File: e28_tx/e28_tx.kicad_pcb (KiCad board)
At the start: 2 copper layers, 40.5 x 56 mm, 25 parts, among them J1 USB_B_Micro, J2 Conn_01x05, J3 Conn_01x04, J4 Conn_01x04, Q1 BC847BS, SW1 SW_Push, SW2 SW_Push, U1 CH340C, U2 me6211c33, U3 ESP32-WROOM-32D, U4 E28-2G4M27S

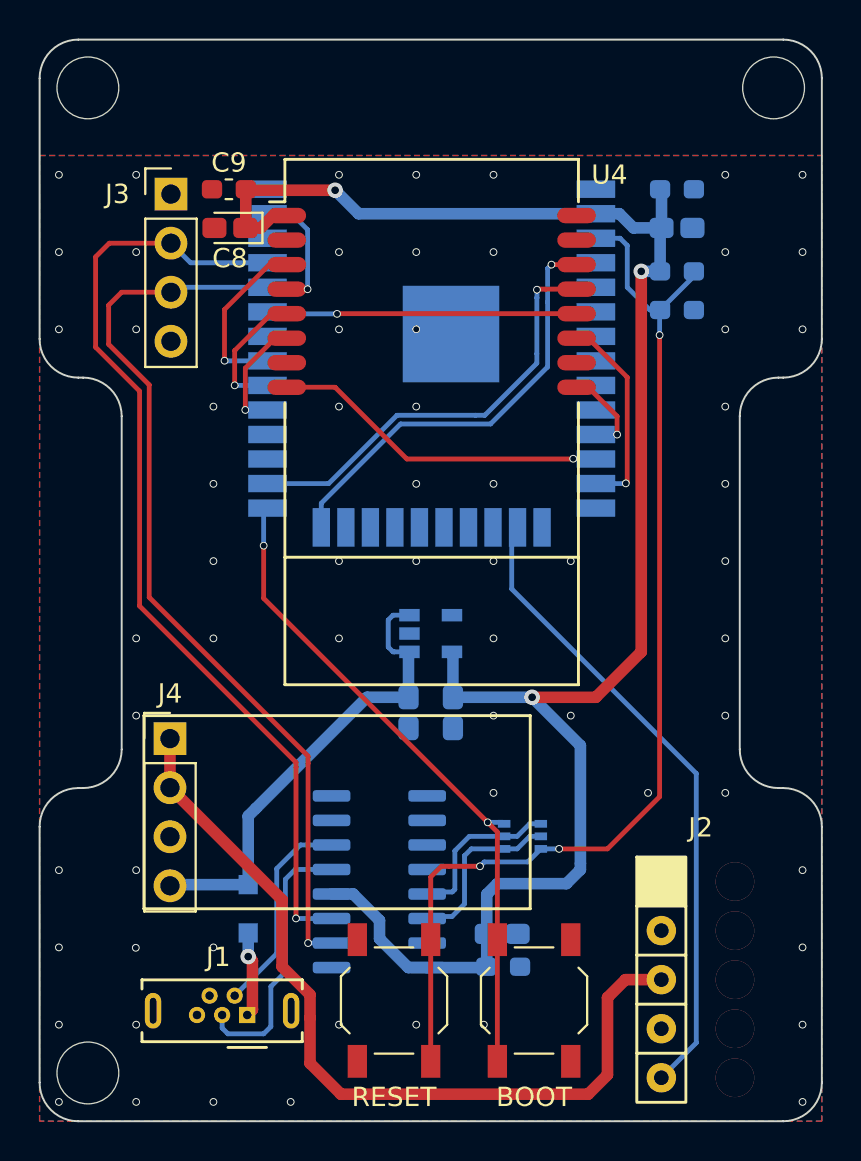
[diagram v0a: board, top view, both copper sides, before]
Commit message: Added minimal RX
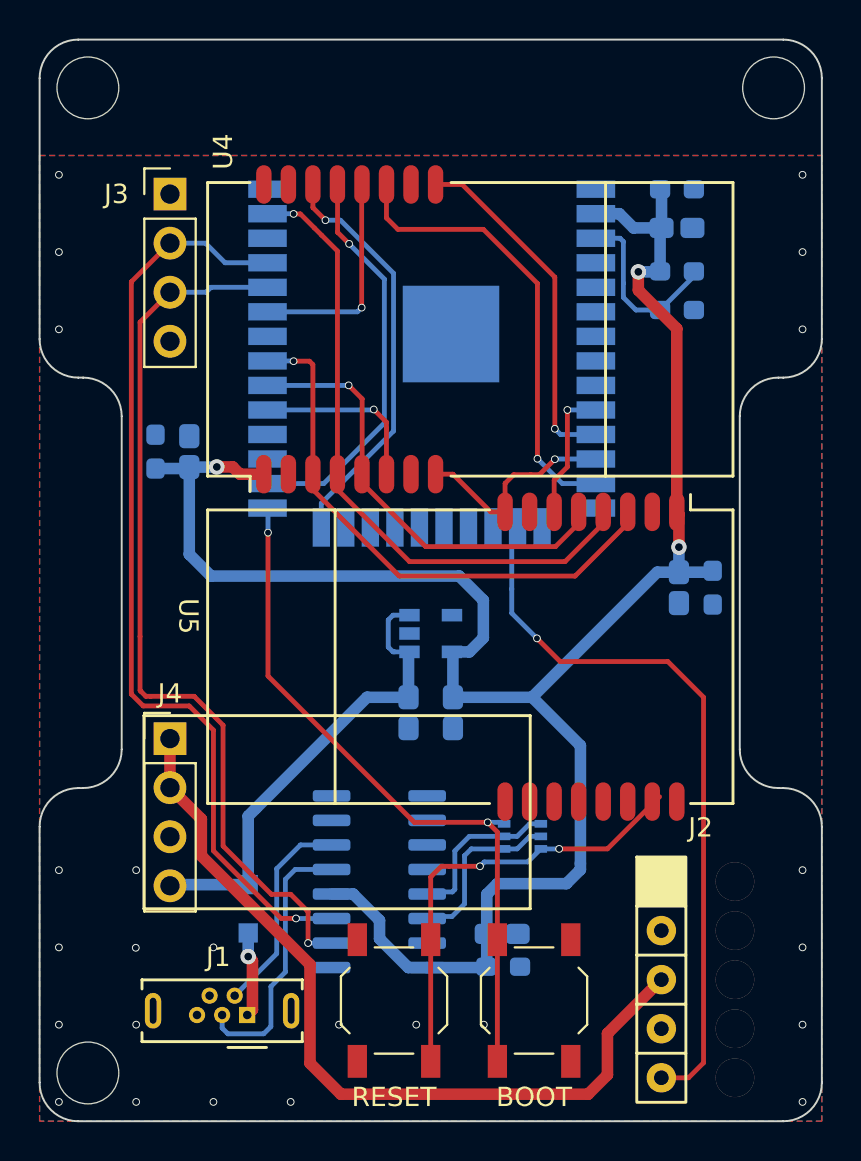
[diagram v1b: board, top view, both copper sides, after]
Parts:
- added C10: 10uF, Capacitor_Tantalum_SMD:CP_EIA-1608-08_AVX-J_Pad1.25x1.05mm_HandSolder, B.Cu at (133.1, 122.4)
- added C11: 100nF, Capacitor_SMD:C_0603_1608Metric_Pad1.05x0.95mm_HandSolder, B.Cu at (134.8, 122.4)
- added U5: E28-2G4M27S, ELRS_lib:E28-2G4M27S, F.Cu at (124.1, 126.0)
- C8, C9: moved to B.Cu
- moved C9 14.1 mm to (106.0, 115.3), turned to 90 degrees
- moved C8 11.8 mm to (107.8, 115.3), turned to 90 degrees
- moved U4 3.01 mm to (120.5, 109.0), turned to 90 degrees
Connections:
- net /DIO1 renamed /DIO11
- net /NSS renamed /NSS1
- J1 pad 4: Net-(J1-Pad4) -> (no net)
- J2 pad 1: Net-(J2-Pad1) -> (no net)
- J2 pad 2: Net-(J2-Pad2) -> (no net)
- J3 pad 1: Net-(J3-Pad1) -> (no net)
- U1 pad 10: Net-(U1-Pad10) -> (no net)
- U1 pad 11: Net-(U1-Pad11) -> (no net)
- U1 pad 12: Net-(U1-Pad12) -> (no net)
- U1 pad 15: Net-(U1-Pad15) -> (no net)
- U1 pad 7: Net-(U1-Pad7) -> (no net)
- U1 pad 8: Net-(U1-Pad8) -> (no net)
- U1 pad 9: Net-(U1-Pad9) -> (no net)
- U3 pad 10: Net-(U3-Pad10) -> /NSS2
- U3 pad 14: Net-(U3-Pad14) -> (no net)
- U3 pad 17: Net-(U3-Pad17) -> (no net)
- U3 pad 18: Net-(U3-Pad18) -> (no net)
- U3 pad 19: Net-(U3-Pad19) -> (no net)
- U3 pad 20: Net-(U3-Pad20) -> (no net)
- U3 pad 21: Net-(U3-Pad21) -> (no net)
- U3 pad 22: Net-(U3-Pad22) -> (no net)
- U3 pad 23: Net-(U3-Pad23) -> (no net)
- U3 pad 24: /DIO2 -> /DIO21
- U3 pad 27: Net-(U3-Pad27) -> /DIO21
- U3 pad 28: Net-(U3-Pad28) -> /DIO12
- U3 pad 32: Net-(U3-Pad32) -> (no net)
- U3 pad 36: Net-(U3-Pad36) -> (no net)
- U3 pad 4: Net-(U3-Pad4) -> (no net)
- U3 pad 5: Net-(U3-Pad5) -> (no net)
- U3 pad 6: Net-(U3-Pad6) -> (no net)
- U3 pad 7: Net-(U3-Pad7) -> (no net)
- U3 pad 8: Net-(U3-Pad8) -> (no net)
- U3 pad 9: Net-(U3-Pad9) -> (no net)
- U4 pad 14: /DIO2 -> /DIO21
- U4 pad 15: Net-(U4-Pad15) -> (no net)
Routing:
- net /MOSI: track 6.58 -> 33.5 mm
- net /RST: track 57.2 -> 32.4 mm, vias 3 -> 2
- net /DIO2: track 22.6 -> 0.00 mm, vias 1 -> 0
- net /DIO21: track 0.00 -> 21.5 mm, vias 0 -> 1
- net /MISO: track 9.07 -> 28.8 mm
- net /SCK: track 6.99 -> 23.2 mm
- net /TXEN: track 4.77 -> 18.3 mm
- net /RESET: track 10.5 -> 23.6 mm
- net +3V3: track 94.4 -> 104.1 mm
- net /NSS2: track 0.00 -> 7.03 mm, vias 0 -> 1
- net /RXEN: track 17.6 -> 11.1 mm
- net /BUSY: track 16.0 -> 11.3 mm
- net /SPORT: track 33.2 -> 37.6 mm, vias 0 -> 1
- net /NSS1: track 6.11 -> 9.13 mm
- net /BOOT: track 34.6 -> 36.7 mm
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
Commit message: Last tweaks and gerber files to min_sx1280 and e28_tx
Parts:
- removed C10: 10uF, Capacitor_Tantalum_SMD:CP_EIA-1608-08_AVX-J_Pad1.25x1.05mm_HandSolder
- removed C11: 100nF, Capacitor_SMD:C_0603_1608Metric_Pad1.05x0.95mm_HandSolder
- removed C3, C5: 2.2uF, Capacitor_Tantalum_SMD:CP_EIA-1608-08_AVX-J_Pad1.25x1.05mm_HandSolder
- removed U2: me6211c33, Package_TO_SOT_SMD:SOT-23-5
- removed U5: E28-2G4M27S, ELRS_lib:E28-2G4M27S
- C8, C9: moved to F.Cu
- H1, H2, H3: renamed from REF**; value MountingHole_3.2mm_M3 -> MountingHole
- moved C9 14.1 mm to (109.8, 101.8), turned to 180 degrees
- moved C8 11.8 mm to (109.8, 103.8), turned to 180 degrees
- moved U4 3.01 mm to (120.3, 112.0), turned to 0 degrees
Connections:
- net /DIO11 renamed /DIO1
- net /NSS1 renamed /NSS
- D1 pad 1: +5V -> /VBAT
- J4 pad 4: +5V -> +3V3
- U3 pad 10: /NSS2 -> (no net)
- U3 pad 24: /DIO21 -> /DIO2
- U3 pad 27: /DIO21 -> (no net)
- U3 pad 28: /DIO12 -> (no net)
- U4 pad 14: /DIO21 -> /DIO2
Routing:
- net /MOSI: track 33.5 -> 6.58 mm
- net +5V: track 24.7 -> 0.00 mm
- net /RST: track 32.4 -> 56.9 mm, vias 2 -> 3
- net /DIO2: track 0.00 -> 22.6 mm, vias 0 -> 1
- net /DIO21: track 21.5 -> 0.00 mm, vias 1 -> 0
- net /MISO: track 28.8 -> 9.07 mm
- net /SCK: track 23.2 -> 6.20 mm
- net /TXEN: track 18.3 -> 4.17 mm
- net /RESET: track 23.6 -> 9.94 mm
- net /NSS2: track 7.03 -> 0.00 mm, vias 1 -> 0
- net /RXEN: track 11.1 -> 17.5 mm
- net +3V3: track 104.1 -> 110.2 mm
- net /BUSY: track 11.3 -> 15.9 mm
- net /SPORT: track 37.6 -> 33.2 mm, vias 1 -> 0
- net /NSS: track 9.13 -> 5.51 mm
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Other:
- board text added: "JLCJLCJLCJLC"
